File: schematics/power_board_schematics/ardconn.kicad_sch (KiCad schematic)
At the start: 2 parts

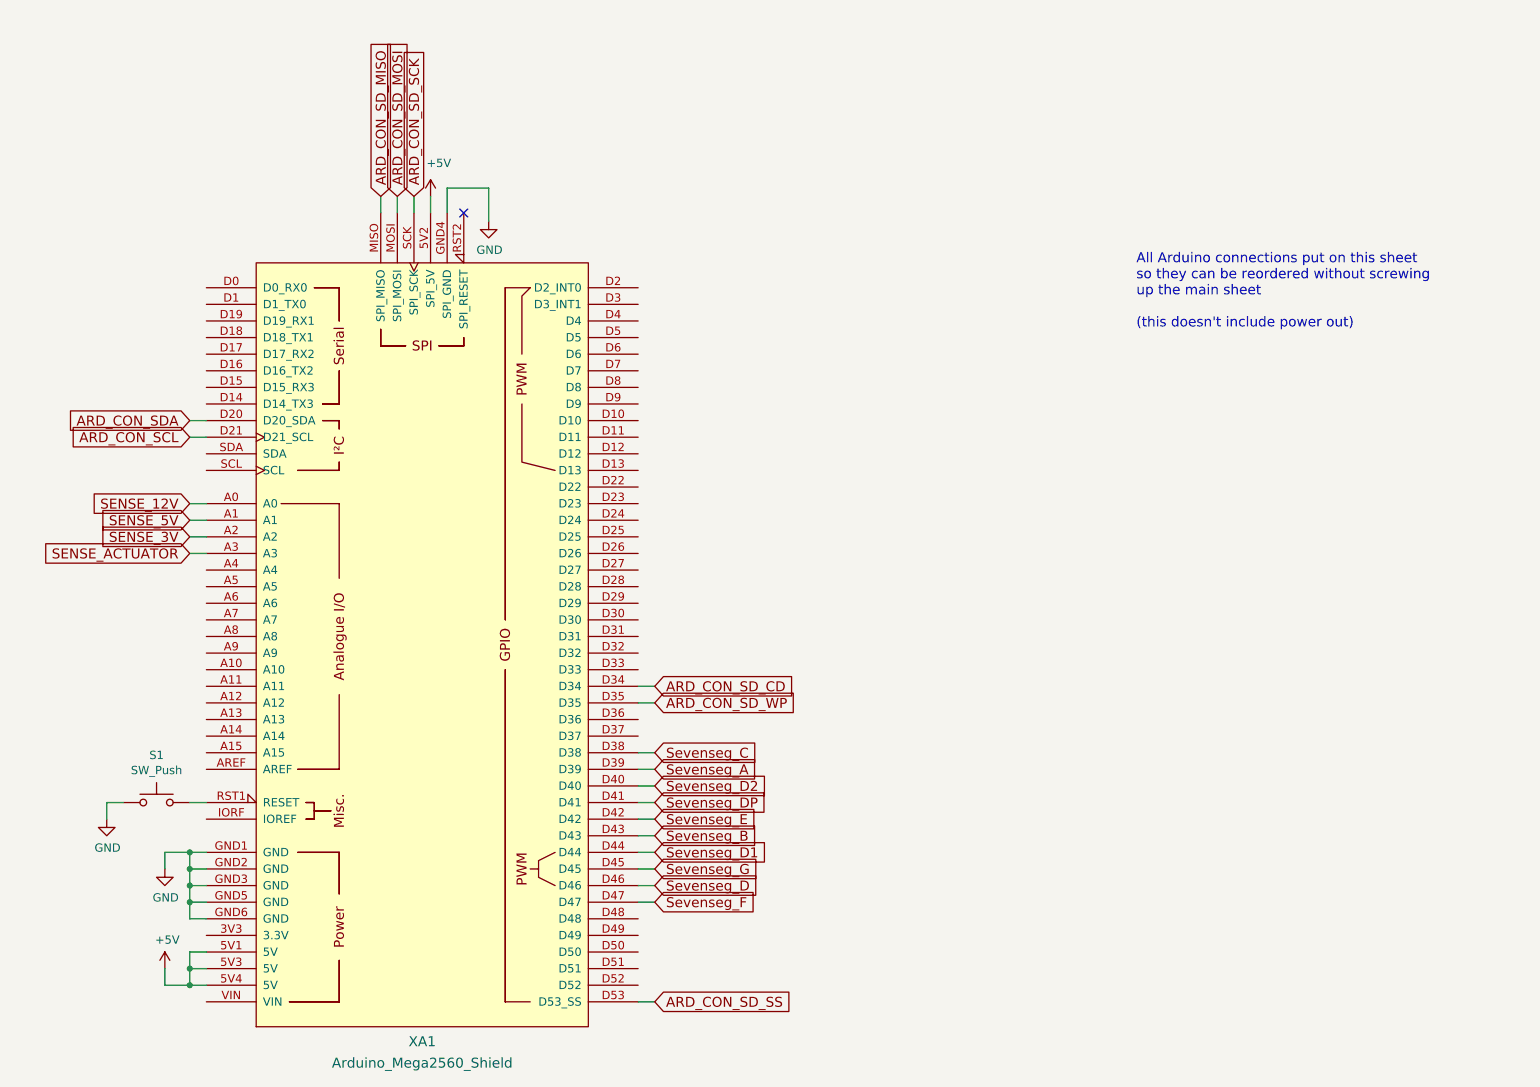
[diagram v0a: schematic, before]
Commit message: Added resistors to transistors, generate pdf and gerbers
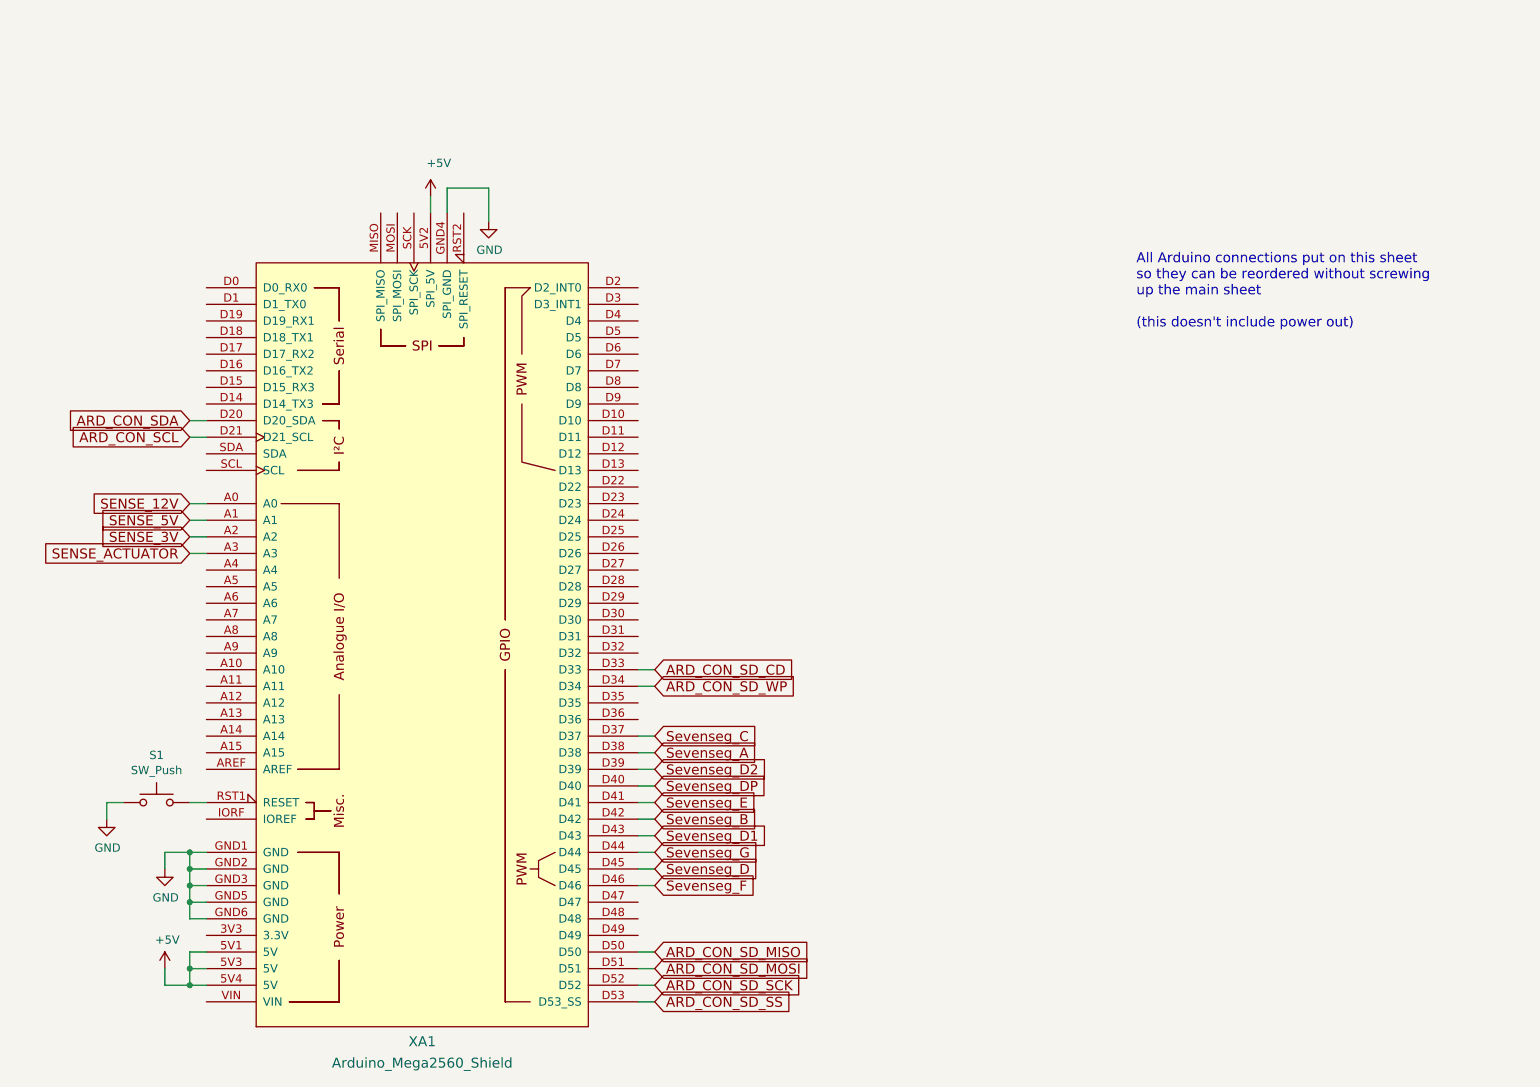
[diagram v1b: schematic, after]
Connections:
- net ARD_CON_SD_CD: now also XA1.D33; no longer XA1.D34
- net ARD_CON_SD_MISO: now also XA1.D50; no longer XA1.MISO (SPI_MISO)
- net ARD_CON_SD_MOSI: now also XA1.D51; no longer XA1.MOSI (SPI_MOSI)
- net ARD_CON_SD_SCK: now also XA1.D52; no longer XA1.SCK (SPI_SCK)
- net ARD_CON_SD_WP: now also XA1.D34; no longer XA1.D35
- net Sevenseg_A: now also XA1.D38; no longer XA1.D39
- net Sevenseg_B: now also XA1.D42; no longer XA1.D43
- net Sevenseg_C: now also XA1.D37; no longer XA1.D38
- net Sevenseg_D: now also XA1.D45; no longer XA1.D46
- net Sevenseg_D1: now also XA1.D43; no longer XA1.D44
- net Sevenseg_D2: now also XA1.D39; no longer XA1.D40
- net Sevenseg_DP: now also XA1.D40; no longer XA1.D41
- net Sevenseg_E: now also XA1.D41; no longer XA1.D42
- net Sevenseg_F: now also XA1.D46; no longer XA1.D47
- net Sevenseg_G: now also XA1.D44; no longer XA1.D45
- no-connect marks 1 -> 0

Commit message: Make 12V traces support higher current, review fixes
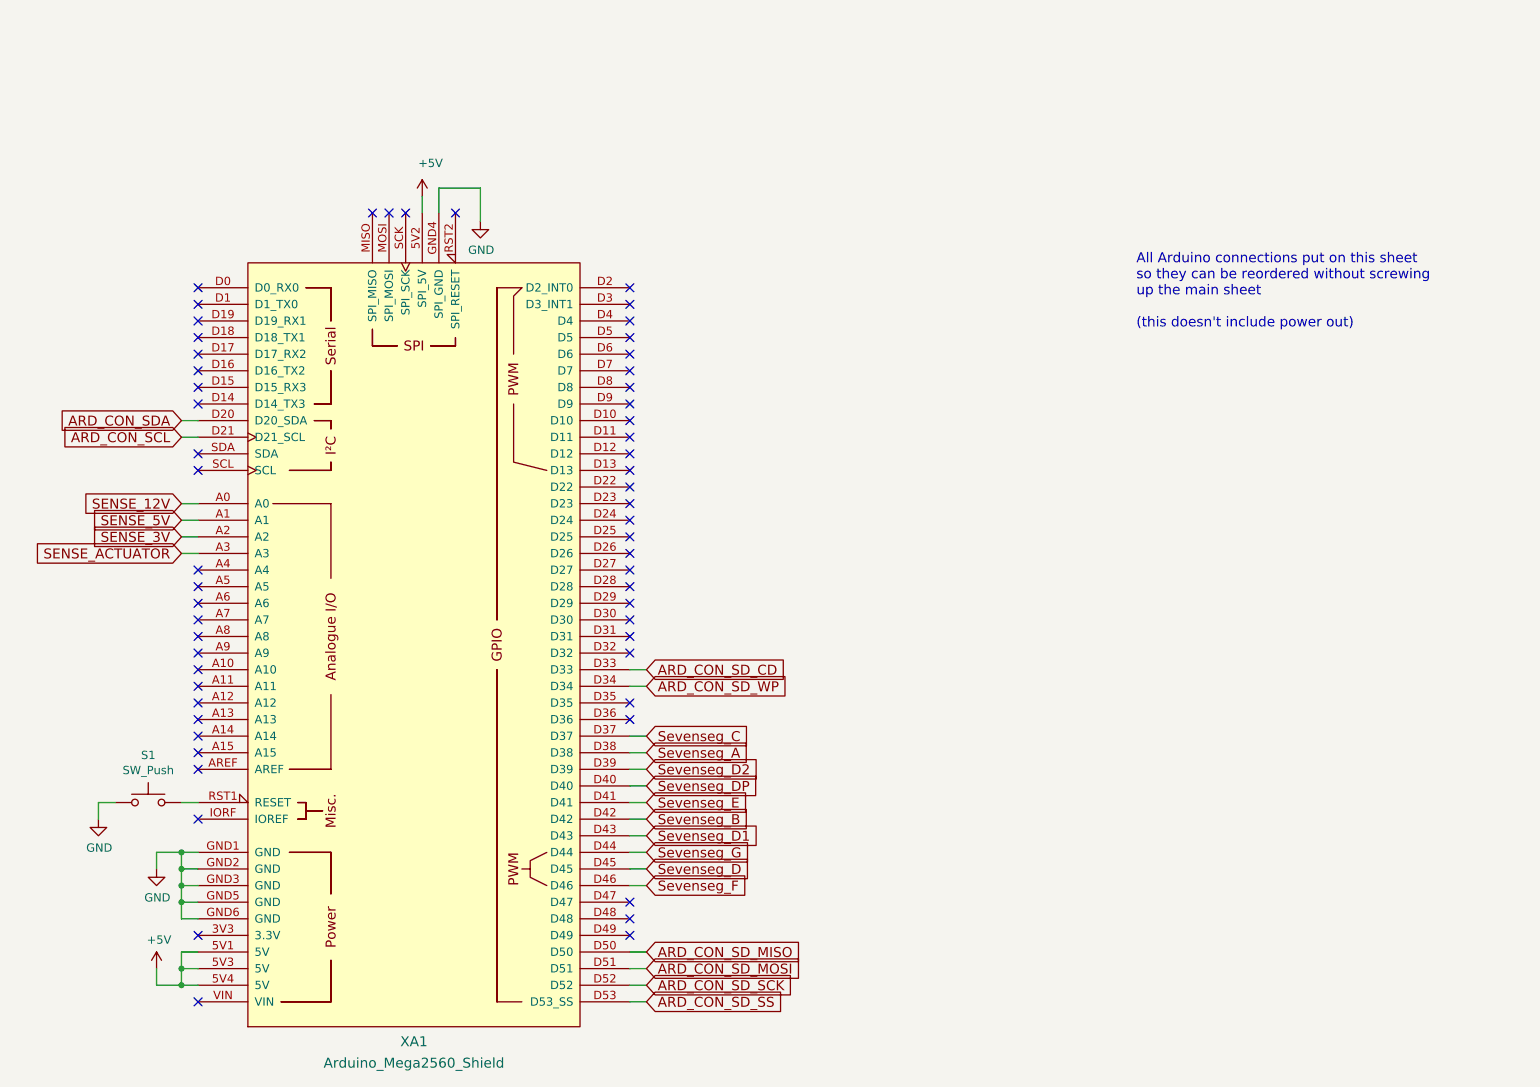
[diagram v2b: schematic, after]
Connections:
- no-connect marks 0 -> 58
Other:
- moved on the sheet: S1, XA1

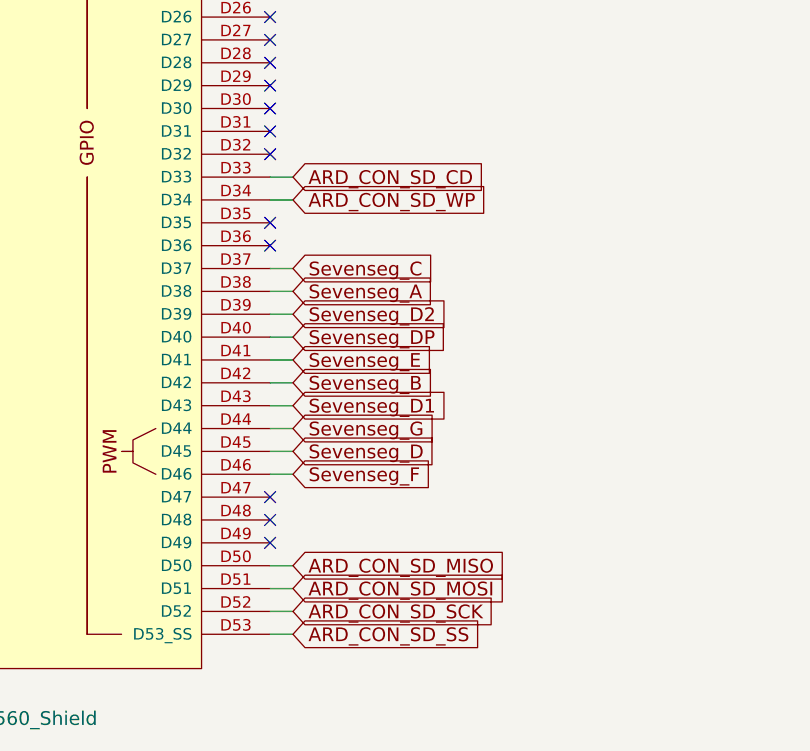
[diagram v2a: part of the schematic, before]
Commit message: Remove SD Card from Towerside Power Board
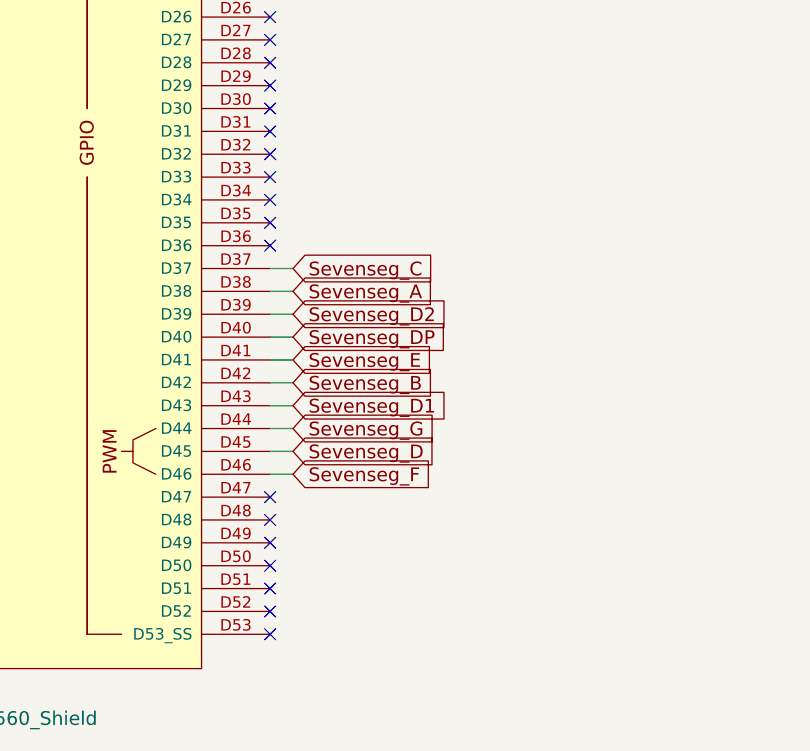
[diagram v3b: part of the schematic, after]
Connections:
- net ARD_CON_SD_CD: no longer names the net of XA1.D33
- net ARD_CON_SD_MISO: no longer names the net of XA1.D50
- net ARD_CON_SD_MOSI: no longer names the net of XA1.D51
- net ARD_CON_SD_SCK: no longer names the net of XA1.D52
- net ARD_CON_SD_SS: no longer names the net of XA1.D53 (D53_SS)
- net ARD_CON_SD_WP: no longer names the net of XA1.D34
- no-connect marks 58 -> 64
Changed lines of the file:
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@@
   (no_connect (at 90.17 49.53))
   (no_connect (at 92.71 49.53))
+  (no_connect (at 127 162.56))
+  (no_connect (at 127 165.1))
+  (no_connect (at 127 167.64))
+  (no_connect (at 127 170.18))
+  (no_connect (at 127 119.38))
+  (no_connect (at 127 121.92))
   (no_connect (at 60.96 86.36))
   (no_connect (at 60.96 78.74))
@@
     (stroke (width 0) (type default) (color 0 0 0 0))
   )
-  (wire (pts (xy 129.54 167.64) (xy 127 167.64))
-    (stroke (width 0) (type default) (color 0 0 0 0))
-  )
   (wire (pts (xy 54.61 147.32) (xy 54.61 149.86))
     (stroke (width 0) (type default) (color 0 0 0 0))
@@
     (stroke (width 0) (type default) (color 0 0 0 0))
   )
-  (wire (pts (xy 127 119.38) (xy 129.54 119.38))
-    (stroke (width 0) (type default) (color 0 0 0 0))
-  )
   (wire (pts (xy 58.42 157.48) (xy 58.42 154.94))
     (stroke (width 0) (type default) (color 0 0 0 0))
@@
     (stroke (width 0) (type default) (color 0 0 0 0))
   )
-  (wire (pts (xy 127 121.92) (xy 129.54 121.92))
-    (stroke (width 0) (type default) (color 0 0 0 0))
-  )
   (wire (pts (xy 129.54 137.16) (xy 127 137.16))
     (stroke (width 0) (type default) (color 0 0 0 0))
@@
     (stroke (width 0) (type default) (color 0 0 0 0))
   )
-  (wire (pts (xy 127 165.1) (xy 129.54 165.1))
-    (stroke (width 0) (type default) (color 0 0 0 0))
-  )
   (wire (pts (xy 58.42 139.7) (xy 60.96 139.7))
     (stroke (width 0) (type default) (color 0 0 0 0))
@@
   )
   (wire (pts (xy 58.42 162.56) (xy 58.42 165.1))
-    (stroke (width 0) (type default) (color 0 0 0 0))
-  )
-  (wire (pts (xy 127 162.56) (xy 129.54 162.56))
-    (stroke (width 0) (type default) (color 0 0 0 0))
-  )
-  (wire (pts (xy 129.54 170.18) (xy 127 170.18))
     (stroke (width 0) (type default) (color 0 0 0 0))
   )
@@
     (effects (font (size 1.524 1.524)) (justify left bottom))
   )
-  (global_label "ARD_CON_SD_SCK" (shape input) (at 129.54 167.64 0) (fields_autoplaced)
-    (effects (font (size 1.524 1.524)) (justify left))
-    (property "Intersheet References" "${INTERSHEET_REFS}" (id 0) (at 312.42 248.92 0)
-      (effects (font (size 1.27 1.27)) hide)
-    )
-  )
   (global_label "Sevenseg_B" (shape input) (at 129.54 142.24 0) (fields_autoplaced)
     (effects (font (size 1.524 1.524)) (justify left))
     (property "Intersheet References" "${INTERSHEET_REFS}" (id 0) (at -99.06 81.28 0)
-      (effects (font (size 1.27 1.27)) hide)
-    )
-  )
-  (global_label "ARD_CON_SD_WP" (shape input) (at 129.54 121.92 0) (fields_autoplaced)
-    (effects (font (size 1.524 1.524)) (justify left))
-    (property "Intersheet References" "${INTERSHEET_REFS}" (id 0) (at -95.25 77.47 0)
       (effects (font (size 1.27 1.27)) hide)
     )
@@
     )
   )
-  (global_label "ARD_CON_SD_CD" (shape input) (at 129.54 119.38 0) (fields_autoplaced)
-    (effects (font (size 1.524 1.524)) (justify left))
-    (property "Intersheet References" "${INTERSHEET_REFS}" (id 0) (at 311.15 163.83 0)
-      (effects (font (size 1.27 1.27)) hide)
-    )
-  )
-  (global_label "ARD_CON_SD_MISO" (shape input) (at 129.54 162.56 0) (fields_autoplaced)
-    (effects (font (size 1.524 1.524)) (justify left))
-    (property "Intersheet References" "${INTERSHEET_REFS}" (id 0) (at 313.69 238.76 0)
-      (effects (font (size 1.27 1.27)) hide)
-    )
-  )
   (global_label "Sevenseg_F" (shape input) (at 129.54 152.4 0) (fields_autoplaced)
     (effects (font (size 1.524 1.524)) (justify left))
@@
     )
   )
-  (global_label "ARD_CON_SD_MOSI" (shape input) (at 129.54 165.1 0) (fields_autoplaced)
-    (effects (font (size 1.524 1.524)) (justify left))
-    (property "Intersheet References" "${INTERSHEET_REFS}" (id 0) (at -99.06 86.36 0)
-      (effects (font (size 1.27 1.27)) hide)
-    )
-  )
   (global_label "Sevenseg_E" (shape input) (at 129.54 139.7 0) (fields_autoplaced)
     (effects (font (size 1.524 1.524)) (justify left))
@@
     )
   )
-  (global_label "ARD_CON_SD_SS" (shape input) (at 129.54 170.18 0) (fields_autoplaced)
-    (effects (font (size 1.524 1.524)) (justify left))
-    (property "Intersheet References" "${INTERSHEET_REFS}" (id 0) (at -99.06 86.36 0)
-      (effects (font (size 1.27 1.27)) hide)
-    )
-  )

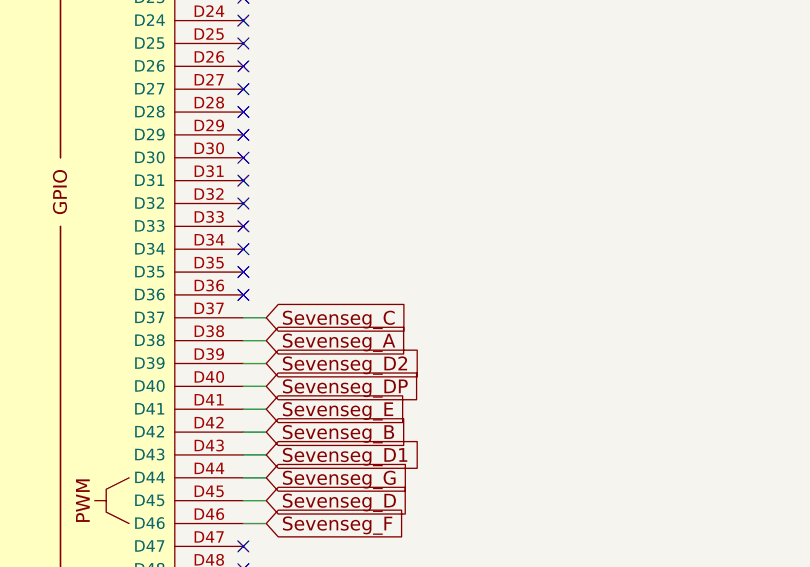
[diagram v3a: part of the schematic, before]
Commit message: Add Client Connection and Arm status indicator LED to Towerside Power Board schematic
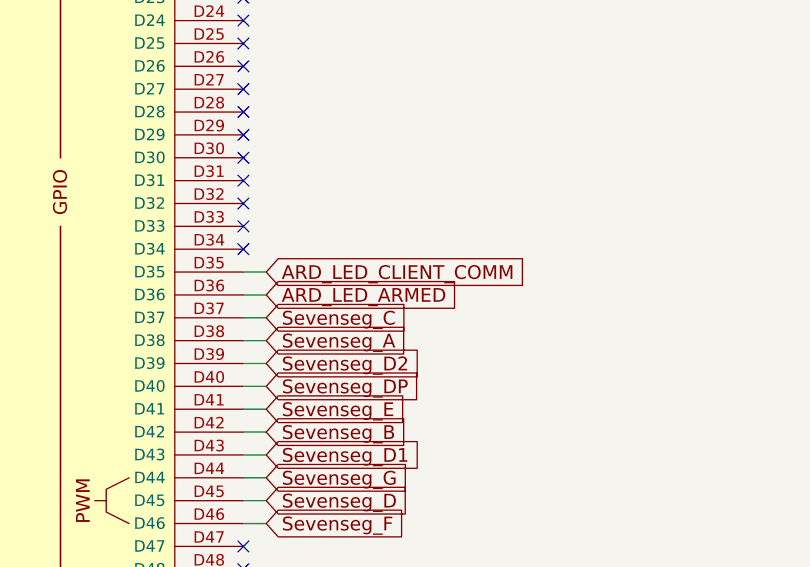
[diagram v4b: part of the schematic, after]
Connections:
- net ARD_LED_CLIENT_COMM: now reaches XA1.D35
- net ARD_LED_ARMED: now reaches XA1.D36
- no-connect marks 64 -> 62
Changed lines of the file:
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@@
   (no_connect (at 60.96 129.54))
   (no_connect (at 60.96 127))
-  (no_connect (at 127 124.46))
-  (no_connect (at 127 127))
   (no_connect (at 60.96 170.18))
   (no_connect (at 60.96 160.02))
@@
     (stroke (width 0) (type default) (color 0 0 0 0))
   )
+  (wire (pts (xy 129.54 124.46) (xy 127 124.46))
+    (stroke (width 0) (type default) (color 0 0 0 0))
+  )
   (wire (pts (xy 58.42 165.1) (xy 60.96 165.1))
     (stroke (width 0) (type default) (color 0 0 0 0))
@@
   )
   (wire (pts (xy 58.42 162.56) (xy 58.42 165.1))
+    (stroke (width 0) (type default) (color 0 0 0 0))
+  )
+  (wire (pts (xy 129.54 127) (xy 127 127))
     (stroke (width 0) (type default) (color 0 0 0 0))
   )
@@
     )
   )
+  (global_label "ARD_LED_ARMED" (shape input) (at 129.54 127 0) (fields_autoplaced)
+    (effects (font (size 1.524 1.524)) (justify left))
+    (property "Intersheet References" "${INTERSHEET_REFS}" (id 0) (at 150.6169 126.9048 0)
+      (effects (font (size 1.524 1.524)) (justify left) hide)
+    )
+  )
   (global_label "ARD_CON_SDA" (shape input) (at 58.42 81.28 180) (fields_autoplaced)
     (effects (font (size 1.524 1.524)) (justify right))
@@
     )
   )
+  (global_label "ARD_LED_CLIENT_COMM" (shape input) (at 129.54 124.46 0) (fields_autoplaced)
+    (effects (font (size 1.524 1.524)) (justify left))
+    (property "Intersheet References" "${INTERSHEET_REFS}" (id 0) (at 158.5272 124.3648 0)
+      (effects (font (size 1.524 1.524)) (justify left) hide)
+    )
+  )
